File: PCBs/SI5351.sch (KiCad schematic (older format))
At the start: 12 parts, among them J4 CAL, Q1 2N7002, Q2 2N7002, U2 Si5351, Y1 25Mhz

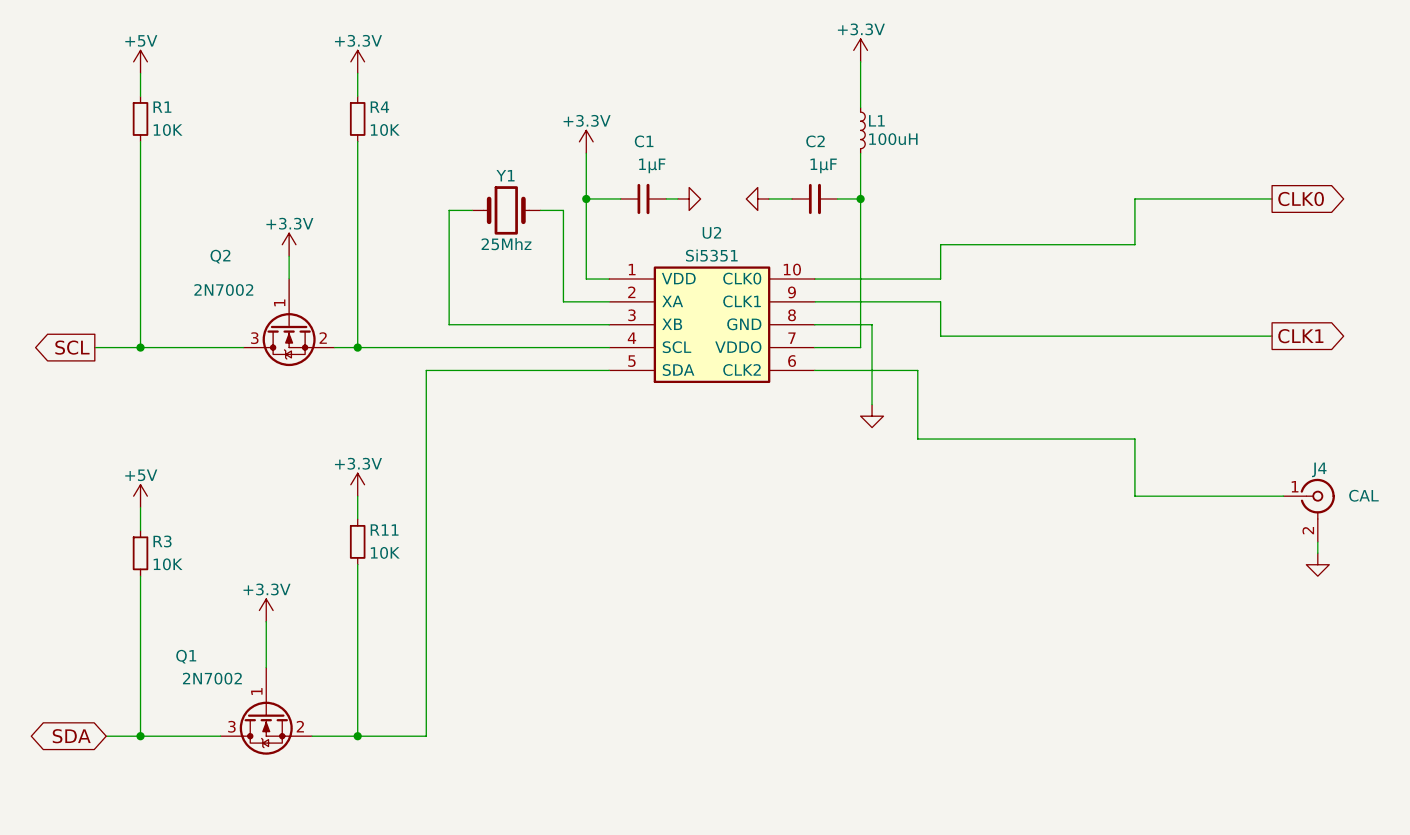
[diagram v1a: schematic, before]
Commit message: discret, simple, CH340E
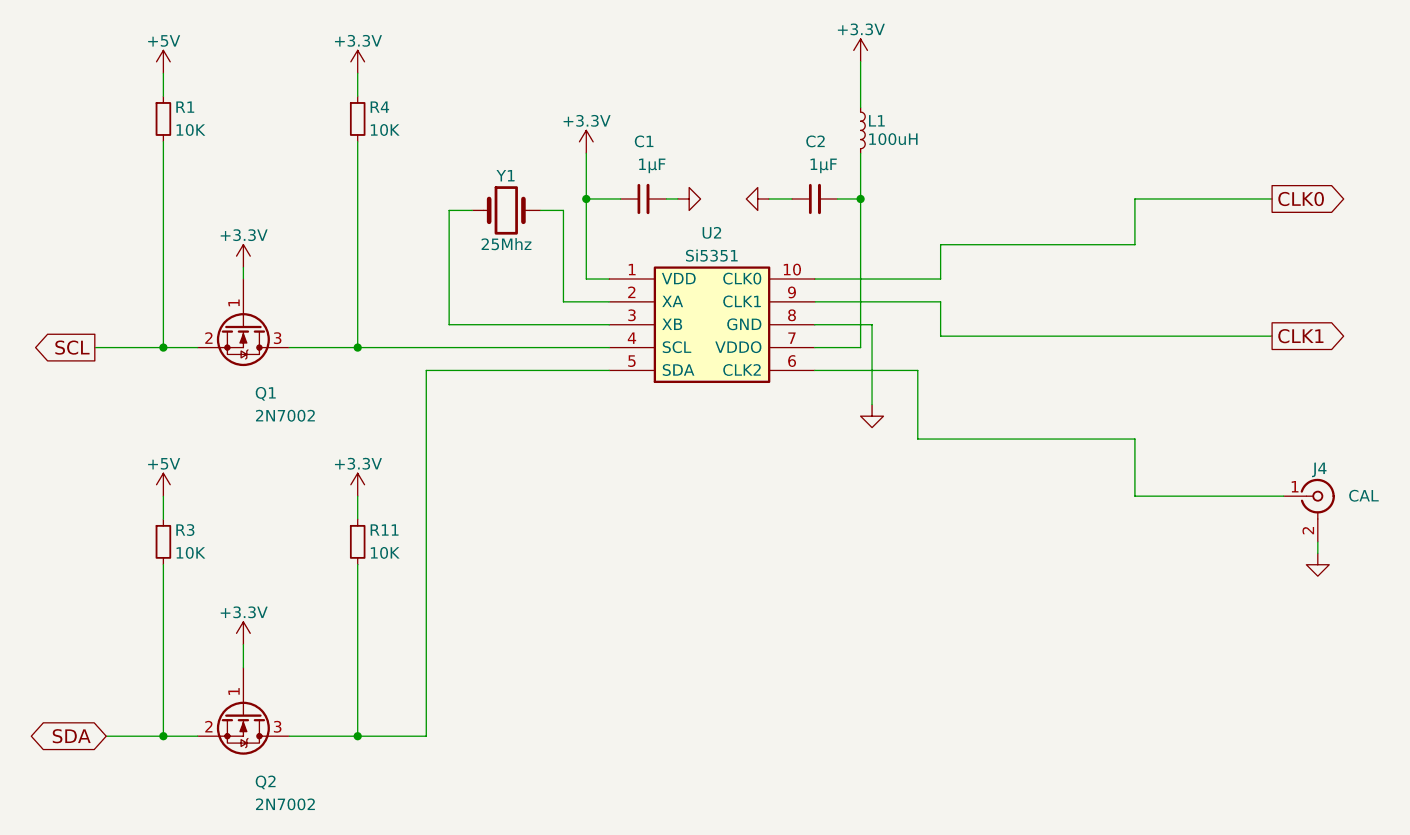
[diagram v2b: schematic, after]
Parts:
- Y1: footprint Crystals:Crystal_SMD_HC49-SD -> Crystals:Crystal_HC49-U_Vertical
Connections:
- net SCL: now also Q1.2 (S); no longer Q2.3 (D)
- net SDA: now also Q2.2 (S); no longer Q1.3 (D)
- net at R4.2, U2.4 (SCL): now also Q1.3 (D); no longer Q2.2 (S)
- net at R11.2, U2.5 (SDA): now also Q2.3 (D); no longer Q1.2 (S)
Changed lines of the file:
@@
 LIBS:BF998
 LIBS:relays
+LIBS:stm32
+LIBS:Interface_USB
+LIBS:Arduino
 LIBS:LCSDR-cache
 EELAYER 25 0
@@
 Comment4 ""
 $EndDescr
-$Comp
-L 2N7002 Q2
-U 1 1 62501FAF
-P 3700 3250
-F 0 "Q2" V 3400 3500 50  0000 L CNN
-F 1 "2N7002" V 3550 3400 50  0000 L CNN
-F 2 "TO_SOT_Packages_SMD:SOT-23" H 3900 3175 50  0001 L CIN
-F 3 "" H 3700 3250 50  0001 L CNN
-	1    3700 3250
-	0    -1   1    0
-$EndComp
-$Comp
-L 2N7002 Q1
-U 1 1 62501FB6
-P 3600 4950
-F 0 "Q1" V 3350 5250 50  0000 L CNN
-F 1 "2N7002" V 3450 5050 50  0000 L CNN
-F 2 "TO_SOT_Packages_SMD:SOT-23" H 3800 4875 50  0001 L CIN
-F 3 "" H 3600 4950 50  0001 L CNN
-	1    3600 4950
-	0    -1   1    0
-$EndComp
 Text GLabel 2900 5050 0    60   BiDi ~ 0
 SDA
 Text GLabel 2850 3350 0    60   Output ~ 0
 SCL
-$Comp
-L +3.3V #PWR6
-U 1 1 62501FC5
-P 3600 4550
-F 0 "#PWR6" H 3600 4400 50  0001 C CNN
-F 1 "+3.3V" H 3600 4690 50  0000 C CNN
-F 2 "" H 3600 4550 50  0001 C CNN
-F 3 "" H 3600 4550 50  0001 C CNN
-	1    3600 4550
-	1    0    0    -1
-$EndComp
 $Comp
 L Si5351 U2
@@
 F 0 "Y1" H 4650 2900 50  0000 C CNN
 F 1 "25Mhz" H 4650 2600 50  0000 C CNN
-F 2 "Crystals:Crystal_SMD_HC49-SD" H 4650 2750 50  0001 C CNN
+F 2 "Crystals:Crystal_HC49-U_Vertical" H 4650 2750 50  0001 C CNN
 F 3 "" H 4650 2750 50  0001 C CNN
 	1    4650 2750
@@
 $EndComp
 $Comp
-L +3.3V #PWR10
+L +3.3V #PWR04
 U 1 1 62501FD9
 P 5000 2500
-F 0 "#PWR10" H 5000 2350 50  0001 C CNN
+F 0 "#PWR04" H 5000 2350 50  0001 C CNN
 F 1 "+3.3V" H 5000 2640 50  0000 C CNN
 F 2 "" H 5000 2500 50  0001 C CNN
@@
 $EndComp
 $Comp
-L GND #PWR14
+L GND #PWR05
 U 1 1 62501FDF
 P 6250 3600
-F 0 "#PWR14" H 6250 3350 50  0001 C CNN
+F 0 "#PWR05" H 6250 3350 50  0001 C CNN
 F 1 "GND" H 6250 3450 50  0001 C CNN
 F 2 "" H 6250 3600 50  0001 C CNN
@@
 $EndComp
 $Comp
-L +3.3V #PWR13
+L +3.3V #PWR06
 U 1 1 62501FE5
 P 6200 2100
-F 0 "#PWR13" H 6200 1950 50  0001 C CNN
+F 0 "#PWR06" H 6200 1950 50  0001 C CNN
 F 1 "+3.3V" H 6200 2240 50  0000 C CNN
 F 2 "" H 6200 2100 50  0001 C CNN
@@
 $EndComp
 $Comp
-L GND #PWR11
+L GND #PWR07
 U 1 1 6250203B
 P 5400 2700
-F 0 "#PWR11" H 5400 2450 50  0001 C CNN
+F 0 "#PWR07" H 5400 2450 50  0001 C CNN
 F 1 "GND" H 5400 2550 50  0001 C CNN
 F 2 "" H 5400 2700 50  0001 C CNN
@@
 $EndComp
 Wire Wire Line
-	2850 3350 3500 3350
-Wire Wire Line
-	2900 5050 3400 5050
-Wire Wire Line
-	3800 5050 4300 5050
+	3700 3350 5100 3350
+Wire Wire Line
+	3700 5050 4300 5050
 Wire Wire Line
 	4800 2750 4900 2750
@@
 Connection ~ 5000 2700
 Wire Wire Line
-	3600 4550 3600 4750
-Wire Wire Line
 	4000 2450 4000 3350
 Connection ~ 4000 3350
@@
 	4300 5050 4300 3450
 $Comp
-L +3.3V #PWR7
-U 1 1 62502072
-P 3700 2950
-F 0 "#PWR7" H 3700 2800 50  0001 C CNN
-F 1 "+3.3V" H 3700 3090 50  0000 C CNN
-F 2 "" H 3700 2950 50  0001 C CNN
-F 3 "" H 3700 2950 50  0001 C CNN
-	1    3700 2950
-	1    0    0    -1
-$EndComp
-Wire Wire Line
-	3700 2950 3700 3050
-$Comp
-L +3.3V #PWR9
+L +3.3V #PWR08
 U 1 1 6250207D
 P 4000 4000
-F 0 "#PWR9" H 4000 3850 50  0001 C CNN
+F 0 "#PWR08" H 4000 3850 50  0001 C CNN
 F 1 "+3.3V" H 4000 4140 50  0000 C CNN
 F 2 "" H 4000 4000 50  0001 C CNN
@@
 	1    0    0    -1
 $EndComp
-Wire Wire Line
-	3050 2450 3050 3350
-Connection ~ 3050 3350
-Wire Wire Line
-	3900 3350 5100 3350
 Wire Wire Line
 	4300 3450 5100 3450
@@
 $EndComp
 $Comp
-L GND #PWR12
+L GND #PWR09
 U 1 1 6253D2ED
 P 5800 2700
-F 0 "#PWR12" H 5800 2450 50  0001 C CNN
+F 0 "#PWR09" H 5800 2450 50  0001 C CNN
 F 1 "GND" H 5800 2550 50  0001 C CNN
 F 2 "" H 5800 2700 50  0001 C CNN
@@
 Text GLabel 8000 2700 2    60   Output ~ 0
 CLK0
-$Comp
-L R_Small R1
-U 1 1 630BFED6
-P 3050 2350
-F 0 "R1" H 3100 2400 50  0000 L CNN
-F 1 "10K" H 3100 2300 50  0000 L CNN
-F 2 "LCSDR:R_1206_0603" H 3050 2350 50  0001 C CNN
-F 3 "" H 3050 2350 50  0001 C CNN
-	1    3050 2350
-	1    0    0    -1
-$EndComp
-$Comp
-L R_Small R3
-U 1 1 630C009D
-P 3050 4250
-F 0 "R3" H 3100 4300 50  0000 L CNN
-F 1 "10K" H 3100 4200 50  0000 L CNN
-F 2 "LCSDR:R_1206_0603" H 3050 4250 50  0001 C CNN
-F 3 "" H 3050 4250 50  0001 C CNN
-	1    3050 4250
-	1    0    0    -1
-$EndComp
-Wire Wire Line
-	3050 4350 3050 5050
-Connection ~ 3050 5050
-$Comp
-L +5V #PWR5
-U 1 1 630C0187
-P 3050 4050
-F 0 "#PWR5" H 3050 3900 50  0001 C CNN
-F 1 "+5V" H 3050 4190 50  0000 C CNN
-F 2 "" H 3050 4050 50  0001 C CNN
-F 3 "" H 3050 4050 50  0001 C CNN
-	1    3050 4050
-	1    0    0    -1
-$EndComp
-Wire Wire Line
-	3050 4050 3050 4150
-$Comp
-L +5V #PWR4
-U 1 1 630C021D
-P 3050 2150
-F 0 "#PWR4" H 3050 2000 50  0001 C CNN
-F 1 "+5V" H 3050 2290 50  0000 C CNN
-F 2 "" H 3050 2150 50  0001 C CNN
-F 3 "" H 3050 2150 50  0001 C CNN
-	1    3050 2150
-	1    0    0    -1
-$EndComp
-Wire Wire Line
-	3050 2150 3050 2250
 $Comp
 L R_Small R4
@@
 $EndComp
 $Comp
-L +3.3V #PWR8
+L +3.3V #PWR010
 U 1 1 630C0393
 P 4000 2150
-F 0 "#PWR8" H 4000 2000 50  0001 C CNN
+F 0 "#PWR010" H 4000 2000 50  0001 C CNN
 F 1 "+3.3V" H 4000 2290 50  0000 C CNN
 F 2 "" H 4000 2150 50  0001 C CNN
@@
 $EndComp
 $Comp
-L GND #PWR15
+L GND #PWR011
 U 1 1 630C6EEC
 P 8200 4250
-F 0 "#PWR15" H 8200 4000 50  0001 C CNN
+F 0 "#PWR011" H 8200 4000 50  0001 C CNN
 F 1 "GND" H 8200 4100 50  0001 C CNN
 F 2 "" H 8200 4250 50  0001 C CNN
@@
 Wire Wire Line
 	8200 4250 8200 4200
+$Comp
+L 2N7002 Q1
+U 1 1 63823E00
+P 3500 3250
+F 0 "Q1" V 3800 3300 50  0000 L CNN
+F 1 "2N7002" V 3900 3300 50  0000 L CNN
+F 2 "TO_SOT_Packages_SMD:SOT-23" H 3700 3175 50  0001 L CIN
+F 3 "" H 3500 3250 50  0001 L CNN
+	1    3500 3250
+	0    1    1    0
+$EndComp
+$Comp
+L +3.3V #PWR012
+U 1 1 63823F32
+P 3500 3000
+F 0 "#PWR012" H 3500 2850 50  0001 C CNN
+F 1 "+3.3V" H 3500 3140 50  0000 C CNN
+F 2 "" H 3500 3000 50  0001 C CNN
+F 3 "" H 3500 3000 50  0001 C CNN
+	1    3500 3000
+	1    0    0    -1
+$EndComp
+Wire Wire Line
+	3500 3000 3500 3050
+Wire Wire Line
+	2850 3350 3300 3350
+$Comp
+L R_Small R1
+U 1 1 63824069
+P 3150 2350
+F 0 "R1" H 3200 2400 50  0000 L CNN
+F 1 "10K" H 3200 2300 50  0000 L CNN
+F 2 "LCSDR:R_1206_0603" H 3150 2350 50  0001 C CNN
+F 3 "" H 3150 2350 50  0001 C CNN
+	1    3150 2350
+	1    0    0    -1
+$EndComp
+Wire Wire Line
+	3150 2450 3150 3350
+Connection ~ 3150 3350
+Wire Wire Line
+	3150 2150 3150 2250
+$Comp
+L +5V #PWR013
+U 1 1 638241C8
+P 3150 2150
+F 0 "#PWR013" H 3150 2000 50  0001 C CNN
+F 1 "+5V" H 3150 2290 50  0000 C CNN
+F 2 "" H 3150 2150 50  0001 C CNN
+F 3 "" H 3150 2150 50  0001 C CNN
+	1    3150 2150
+	1    0    0    -1
+$EndComp
+$Comp
+L 2N7002 Q2
+U 1 1 638242E2
+P 3500 4950
+F 0 "Q2" V 3800 5000 50  0000 L CNN
+F 1 "2N7002" V 3900 5000 50  0000 L CNN
+F 2 "TO_SOT_Packages_SMD:SOT-23" H 3700 4875 50  0001 L CIN
+F 3 "" H 3500 4950 50  0001 L CNN
+	1    3500 4950
+	0    1    1    0
+$EndComp
+Wire Wire Line
+	2900 5050 3300 5050
+Connection ~ 3150 5050
+Wire Wire Line
+	3150 5050 3150 4300
+$Comp
+L R_Small R3
+U 1 1 638246FB
+P 3150 4200
+F 0 "R3" H 3200 4250 50  0000 L CNN
+F 1 "10K" H 3200 4150 50  0000 L CNN
+F 2 "LCSDR:R_1206_0603" H 3150 4200 50  0001 C CNN
+F 3 "" H 3150 4200 50  0001 C CNN
+	1    3150 4200
+	1    0    0    -1
+$EndComp
+$Comp
+L +5V #PWR014
+U 1 1 6382473D
+P 3150 4000
+F 0 "#PWR014" H 3150 3850 50  0001 C CNN
+F 1 "+5V" H 3150 4140 50  0000 C CNN
+F 2 "" H 3150 4000 50  0001 C CNN
+F 3 "" H 3150 4000 50  0001 C CNN
+	1    3150 4000
+	1    0    0    -1
+$EndComp
+Wire Wire Line
+	3150 4000 3150 4100
+$Comp
+L +3.3V #PWR015
+U 1 1 638247BA
+P 3500 4650
+F 0 "#PWR015" H 3500 4500 50  0001 C CNN
+F 1 "+3.3V" H 3500 4790 50  0000 C CNN
+F 2 "" H 3500 4650 50  0001 C CNN
+F 3 "" H 3500 4650 50  0001 C CNN
+	1    3500 4650
+	1    0    0    -1
+$EndComp
+Wire Wire Line
+	3500 4650 3500 4750
 $EndSCHEMATC

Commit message: INIT project, si5351 generate properly frequency
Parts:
- L1: footprint Resistors_THT:R_Axial_DIN0207_L6.3mm_D2.5mm_P10.16mm_Horizontal -> Choke_Axial_ThroughHole:Choke_Horizontal_RM10mm
- R1, R11, R3, R4: footprint LCSDR:R_1206_0603 -> Resistors_SMD:R_0603_HandSoldering
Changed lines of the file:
@@
 $Descr A4 11693 8268
 encoding utf-8
-Sheet 2 8
+Sheet 2 7
 Title ""
 Date ""
@@
 $EndComp
 $Comp
-L +3.3V #PWR04
+L +3.3V #PWR02
 U 1 1 62501FD9
 P 5000 2500
-F 0 "#PWR04" H 5000 2350 50  0001 C CNN
+F 0 "#PWR02" H 5000 2350 50  0001 C CNN
 F 1 "+3.3V" H 5000 2640 50  0000 C CNN
 F 2 "" H 5000 2500 50  0001 C CNN
@@
 $EndComp
 $Comp
-L GND #PWR05
+L GND #PWR03
 U 1 1 62501FDF
 P 6250 3600
-F 0 "#PWR05" H 6250 3350 50  0001 C CNN
+F 0 "#PWR03" H 6250 3350 50  0001 C CNN
 F 1 "GND" H 6250 3450 50  0001 C CNN
 F 2 "" H 6250 3600 50  0001 C CNN
@@
 $EndComp
 $Comp
-L +3.3V #PWR06
+L +3.3V #PWR04
 U 1 1 62501FE5
 P 6200 2100
-F 0 "#PWR06" H 6200 1950 50  0001 C CNN
+F 0 "#PWR04" H 6200 1950 50  0001 C CNN
 F 1 "+3.3V" H 6200 2240 50  0000 C CNN
 F 2 "" H 6200 2100 50  0001 C CNN
@@
 $EndComp
 $Comp
-L GND #PWR07
+L GND #PWR05
 U 1 1 6250203B
 P 5400 2700
-F 0 "#PWR07" H 5400 2450 50  0001 C CNN
+F 0 "#PWR05" H 5400 2450 50  0001 C CNN
 F 1 "GND" H 5400 2550 50  0001 C CNN
 F 2 "" H 5400 2700 50  0001 C CNN
@@
 	4300 5050 4300 3450
 $Comp
-L +3.3V #PWR08
+L +3.3V #PWR06
 U 1 1 6250207D
 P 4000 4000
-F 0 "#PWR08" H 4000 3850 50  0001 C CNN
+F 0 "#PWR06" H 4000 3850 50  0001 C CNN
 F 1 "+3.3V" H 4000 4140 50  0000 C CNN
 F 2 "" H 4000 4000 50  0001 C CNN
@@
 F 0 "L1" H 6230 2440 50  0000 L CNN
 F 1 "100uH" H 6230 2360 50  0000 L CNN
-F 2 "Resistors_THT:R_Axial_DIN0207_L6.3mm_D2.5mm_P10.16mm_Horizontal" H 6200 2400 50  0001 C CNN
+F 2 "Choke_Axial_ThroughHole:Choke_Horizontal_RM10mm" H 6200 2400 50  0001 C CNN
 F 3 "" H 6200 2400 50  0001 C CNN
 	1    6200 2400
@@
 $EndComp
 $Comp
-L GND #PWR09
+L GND #PWR07
 U 1 1 6253D2ED
 P 5800 2700
-F 0 "#PWR09" H 5800 2450 50  0001 C CNN
+F 0 "#PWR07" H 5800 2450 50  0001 C CNN
 F 1 "GND" H 5800 2550 50  0001 C CNN
 F 2 "" H 5800 2700 50  0001 C CNN
@@
 F 0 "R4" H 4050 2400 50  0000 L CNN
 F 1 "10K" H 4050 2300 50  0000 L CNN
-F 2 "LCSDR:R_1206_0603" H 4000 2350 50  0001 C CNN
+F 2 "Resistors_SMD:R_0603_HandSoldering" H 4000 2350 50  0001 C CNN
 F 3 "" H 4000 2350 50  0001 C CNN
 	1    4000 2350
@@
 $EndComp
 $Comp
-L +3.3V #PWR010
+L +3.3V #PWR08
 U 1 1 630C0393
 P 4000 2150
-F 0 "#PWR010" H 4000 2000 50  0001 C CNN
+F 0 "#PWR08" H 4000 2000 50  0001 C CNN
 F 1 "+3.3V" H 4000 2290 50  0000 C CNN
 F 2 "" H 4000 2150 50  0001 C CNN
@@
 F 0 "R11" H 4050 4250 50  0000 L CNN
 F 1 "10K" H 4050 4150 50  0000 L CNN
-F 2 "LCSDR:R_1206_0603" H 4000 4200 50  0001 C CNN
+F 2 "Resistors_SMD:R_0603_HandSoldering" H 4000 4200 50  0001 C CNN
 F 3 "" H 4000 4200 50  0001 C CNN
 	1    4000 4200
@@
 $EndComp
 $Comp
-L GND #PWR011
+L GND #PWR09
 U 1 1 630C6EEC
 P 8200 4250
-F 0 "#PWR011" H 8200 4000 50  0001 C CNN
+F 0 "#PWR09" H 8200 4000 50  0001 C CNN
 F 1 "GND" H 8200 4100 50  0001 C CNN
 F 2 "" H 8200 4250 50  0001 C CNN
@@
 $EndComp
 $Comp
-L +3.3V #PWR012
+L +3.3V #PWR010
 U 1 1 63823F32
 P 3500 3000
-F 0 "#PWR012" H 3500 2850 50  0001 C CNN
+F 0 "#PWR010" H 3500 2850 50  0001 C CNN
 F 1 "+3.3V" H 3500 3140 50  0000 C CNN
 F 2 "" H 3500 3000 50  0001 C CNN
@@
 F 0 "R1" H 3200 2400 50  0000 L CNN
 F 1 "10K" H 3200 2300 50  0000 L CNN
-F 2 "LCSDR:R_1206_0603" H 3150 2350 50  0001 C CNN
+F 2 "Resistors_SMD:R_0603_HandSoldering" H 3150 2350 50  0001 C CNN
 F 3 "" H 3150 2350 50  0001 C CNN
 	1    3150 2350
@@
 	3150 2150 3150 2250
 $Comp
-L +5V #PWR013
+L +5V #PWR011
 U 1 1 638241C8
 P 3150 2150
-F 0 "#PWR013" H 3150 2000 50  0001 C CNN
+F 0 "#PWR011" H 3150 2000 50  0001 C CNN
 F 1 "+5V" H 3150 2290 50  0000 C CNN
 F 2 "" H 3150 2150 50  0001 C CNN
@@
 F 0 "R3" H 3200 4250 50  0000 L CNN
 F 1 "10K" H 3200 4150 50  0000 L CNN
-F 2 "LCSDR:R_1206_0603" H 3150 4200 50  0001 C CNN
+F 2 "Resistors_SMD:R_0603_HandSoldering" H 3150 4200 50  0001 C CNN
 F 3 "" H 3150 4200 50  0001 C CNN
 	1    3150 4200
@@
 $EndComp
 $Comp
-L +5V #PWR014
+L +5V #PWR012
 U 1 1 6382473D
 P 3150 4000
-F 0 "#PWR014" H 3150 3850 50  0001 C CNN
+F 0 "#PWR012" H 3150 3850 50  0001 C CNN
 F 1 "+5V" H 3150 4140 50  0000 C CNN
 F 2 "" H 3150 4000 50  0001 C CNN
@@
 	3150 4000 3150 4100
 $Comp
-L +3.3V #PWR015
+L +3.3V #PWR013
 U 1 1 638247BA
 P 3500 4650
-F 0 "#PWR015" H 3500 4500 50  0001 C CNN
+F 0 "#PWR013" H 3500 4500 50  0001 C CNN
 F 1 "+3.3V" H 3500 4790 50  0000 C CNN
 F 2 "" H 3500 4650 50  0001 C CNN

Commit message: add printout, finish PCB, add LM7805
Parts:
- removed J4: CAL, LCSDR:U.FL_Molex_MCRF_73412-0110_Vertical, symbol Conn_Coaxial
- added J3: Calibration, Pin_Headers:Pin_Header_Straight_1x02_Pitch2.54mm, symbol Conn_01x02
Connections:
- net GND: now also J3.2 (Pin_2)
- net at U2.6 (CLK2): now also J3.1 (Pin_1)
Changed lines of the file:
@@
 $EndComp
 $Comp
-L +3.3V #PWR02
+L +3.3V #PWR8
 U 1 1 62501FD9
 P 5000 2500
-F 0 "#PWR02" H 5000 2350 50  0001 C CNN
+F 0 "#PWR8" H 5000 2350 50  0001 C CNN
 F 1 "+3.3V" H 5000 2640 50  0000 C CNN
 F 2 "" H 5000 2500 50  0001 C CNN
@@
 $EndComp
 $Comp
-L GND #PWR03
+L GND #PWR12
 U 1 1 62501FDF
 P 6250 3600
-F 0 "#PWR03" H 6250 3350 50  0001 C CNN
+F 0 "#PWR12" H 6250 3350 50  0001 C CNN
 F 1 "GND" H 6250 3450 50  0001 C CNN
 F 2 "" H 6250 3600 50  0001 C CNN
@@
 $EndComp
 $Comp
-L +3.3V #PWR04
+L +3.3V #PWR11
 U 1 1 62501FE5
 P 6200 2100
-F 0 "#PWR04" H 6200 1950 50  0001 C CNN
+F 0 "#PWR11" H 6200 1950 50  0001 C CNN
 F 1 "+3.3V" H 6200 2240 50  0000 C CNN
 F 2 "" H 6200 2100 50  0001 C CNN
@@
 $EndComp
 $Comp
-L GND #PWR05
+L GND #PWR9
 U 1 1 6250203B
 P 5400 2700
-F 0 "#PWR05" H 5400 2450 50  0001 C CNN
+F 0 "#PWR9" H 5400 2450 50  0001 C CNN
 F 1 "GND" H 5400 2550 50  0001 C CNN
 F 2 "" H 5400 2700 50  0001 C CNN
@@
 	4300 5050 4300 3450
 $Comp
-L +3.3V #PWR06
+L +3.3V #PWR7
 U 1 1 6250207D
 P 4000 4000
-F 0 "#PWR06" H 4000 3850 50  0001 C CNN
+F 0 "#PWR7" H 4000 3850 50  0001 C CNN
 F 1 "+3.3V" H 4000 4140 50  0000 C CNN
 F 2 "" H 4000 4000 50  0001 C CNN
@@
 $EndComp
 $Comp
-L GND #PWR07
+L GND #PWR10
 U 1 1 6253D2ED
 P 5800 2700
-F 0 "#PWR07" H 5800 2450 50  0001 C CNN
+F 0 "#PWR10" H 5800 2450 50  0001 C CNN
 F 1 "GND" H 5800 2550 50  0001 C CNN
 F 2 "" H 5800 2700 50  0001 C CNN
@@
 $EndComp
 $Comp
-L +3.3V #PWR08
+L +3.3V #PWR6
 U 1 1 630C0393
 P 4000 2150
-F 0 "#PWR08" H 4000 2000 50  0001 C CNN
+F 0 "#PWR6" H 4000 2000 50  0001 C CNN
 F 1 "+3.3V" H 4000 2290 50  0000 C CNN
 F 2 "" H 4000 2150 50  0001 C CNN
@@
 Connection ~ 4000 5050
 $Comp
-L Conn_Coaxial J4
-U 1 1 630C6EE5
-P 8200 4000
-F 0 "J4" H 8210 4120 50  0000 C CNN
-F 1 "CAL" H 8400 4000 50  0000 C CNN
-F 2 "LCSDR:U.FL_Molex_MCRF_73412-0110_Vertical" H 8200 4000 50  0001 C CNN
-F 3 "" H 8200 4000 50  0001 C CNN
-	1    8200 4000
-	1    0    0    -1
-$EndComp
-$Comp
-L GND #PWR09
+L GND #PWR13
 U 1 1 630C6EEC
-P 8200 4250
-F 0 "#PWR09" H 8200 4000 50  0001 C CNN
-F 1 "GND" H 8200 4100 50  0001 C CNN
-F 2 "" H 8200 4250 50  0001 C CNN
-F 3 "" H 8200 4250 50  0001 C CNN
-	1    8200 4250
+P 7800 4200
+F 0 "#PWR13" H 7800 3950 50  0001 C CNN
+F 1 "GND" H 7800 4050 50  0001 C CNN
+F 2 "" H 7800 4200 50  0001 C CNN
+F 3 "" H 7800 4200 50  0001 C CNN
+	1    7800 4200
 	-1   0    0    -1
 $EndComp
 Wire Wire Line
-	8200 4250 8200 4200
+	7800 4100 7800 4200
 $Comp
 L 2N7002 Q1
@@
 $EndComp
 $Comp
-L +3.3V #PWR010
+L +3.3V #PWR4
 U 1 1 63823F32
 P 3500 3000
-F 0 "#PWR010" H 3500 2850 50  0001 C CNN
+F 0 "#PWR4" H 3500 2850 50  0001 C CNN
 F 1 "+3.3V" H 3500 3140 50  0000 C CNN
 F 2 "" H 3500 3000 50  0001 C CNN
@@
 	3150 2150 3150 2250
 $Comp
-L +5V #PWR011
+L +5V #PWR2
 U 1 1 638241C8
 P 3150 2150
-F 0 "#PWR011" H 3150 2000 50  0001 C CNN
+F 0 "#PWR2" H 3150 2000 50  0001 C CNN
 F 1 "+5V" H 3150 2290 50  0000 C CNN
 F 2 "" H 3150 2150 50  0001 C CNN
@@
 $EndComp
 $Comp
-L +5V #PWR012
+L +5V #PWR3
 U 1 1 6382473D
 P 3150 4000
-F 0 "#PWR012" H 3150 3850 50  0001 C CNN
+F 0 "#PWR3" H 3150 3850 50  0001 C CNN
 F 1 "+5V" H 3150 4140 50  0000 C CNN
 F 2 "" H 3150 4000 50  0001 C CNN
@@
 	3150 4000 3150 4100
 $Comp
-L +3.3V #PWR013
+L +3.3V #PWR5
 U 1 1 638247BA
 P 3500 4650
-F 0 "#PWR013" H 3500 4500 50  0001 C CNN
+F 0 "#PWR5" H 3500 4500 50  0001 C CNN
 F 1 "+3.3V" H 3500 4790 50  0000 C CNN
 F 2 "" H 3500 4650 50  0001 C CNN
@@
 Wire Wire Line
 	3500 4650 3500 4750
+$Comp
+L Conn_01x02 J3
+U 1 1 63A8716E
+P 8250 4000
+F 0 "J3" H 8250 4100 50  0000 C CNN
+F 1 "Calibration" H 8250 3800 50  0000 C CNN
+F 2 "Pin_Headers:Pin_Header_Straight_1x02_Pitch2.54mm" H 8250 4000 50  0001 C CNN
+F 3 "" H 8250 4000 50  0001 C CNN
+	1    8250 4000
+	1    0    0    -1
+$EndComp
+Wire Wire Line
+	7800 4100 8050 4100
 $EndSCHEMATC
